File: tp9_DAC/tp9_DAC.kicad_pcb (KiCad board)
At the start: 2 copper layers, 24 parts, among them J2 BAT1, U1 NE555P, U2 NE555P

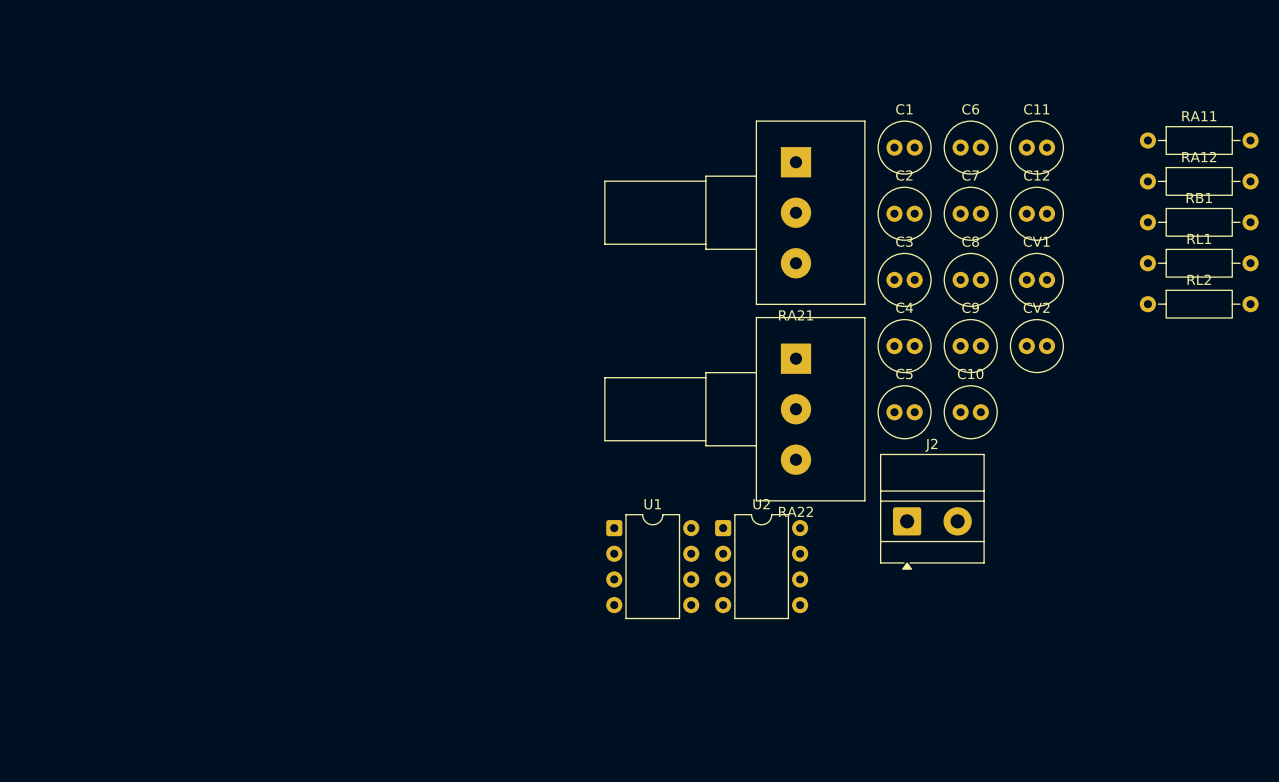
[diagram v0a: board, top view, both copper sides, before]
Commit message: update_tp9_DAC
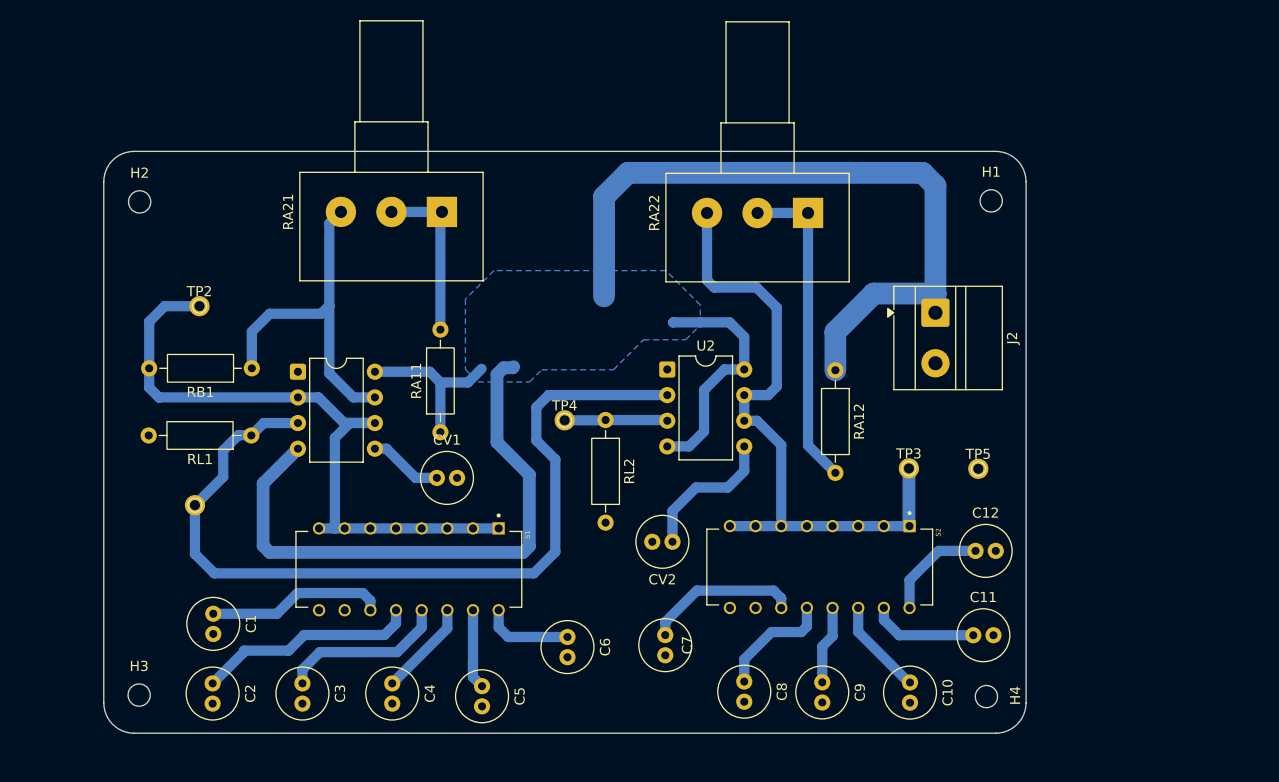
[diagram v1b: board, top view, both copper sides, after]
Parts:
- added H1: MountingHole, MountingHole:MountingHole_2.2mm_M2_DIN965, F.Cu at (168.8, 57.3)
- added H2: MountingHole, MountingHole:MountingHole_2.2mm_M2_DIN965, F.Cu at (84.5, 57.4)
- added H3: MountingHole, MountingHole:MountingHole_2.2mm_M2_DIN965, F.Cu at (84.5, 106.2)
- added H4: MountingHole, MountingHole:MountingHole_2.2mm_M2_DIN965, F.Cu at (168.3, 106.3)
- added S1: ADE0804, ADE0804:SW_ADE0804, F.Cu at (111.2, 93.8)
- added S2: ADE0804, ADE0804:SW_ADE0804, F.Cu at (151.8, 93.5)
- added TP1: TestPoint, TestPoint:TestPoint_THTPad_D1.0mm_Drill0.5mm, F.Cu at (90.0, 87.4)
- added TP2: TestPoint, TestPoint:TestPoint_THTPad_D1.0mm_Drill0.5mm, F.Cu at (90.5, 67.7)
- added TP3: TestPoint, TestPoint:TestPoint_THTPad_D1.0mm_Drill0.5mm, F.Cu at (160.7, 83.8)
- added TP4: TestPoint, TestPoint:TestPoint_THTPad_D1.0mm_Drill0.5mm, F.Cu at (126.6, 79.0)
- added TP5: TestPoint, TestPoint:TestPoint_THTPad_D1.0mm_Drill0.5mm, F.Cu at (167.6, 83.8)
- moved RL1 90.4 mm to (95.6, 80.5), turned to 180 degrees
- moved RB1 89.9 mm to (95.6, 73.8), turned to 180 degrees
- moved C2 82.0 mm to (91.8, 105.0), turned to -90 degrees
- moved C1 81.7 mm to (91.8, 98.2), turned to -90 degrees
- moved RA11 75.8 mm to (114.3, 80.2), turned to 90 degrees
- moved C3 70.9 mm to (100.6, 105.0), turned to -90 degrees
- moved C6 62.1 mm to (126.9, 100.4), turned to -90 degrees
- moved CV1 61.6 mm to (114.0, 84.7)
- moved C4 59.9 mm to (109.5, 105.0), turned to -90 degrees
- moved RL2 54.9 mm to (130.7, 79.0), turned to -90 degrees
- moved C7 50.9 mm to (136.6, 100.3), turned to -90 degrees
- moved C5 49.0 mm to (118.4, 105.3), turned to -90 degrees
- moved C11 48.6 mm to (167.1, 100.3)
- moved C8 45.2 mm to (144.4, 104.9), turned to -90 degrees
- moved CV2 40.1 mm to (137.3, 91.0), turned to 180 degrees
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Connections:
- C1 pad 1: unconnected-(C1-Pad1) -> Net-(C1-Pad1)
- C1 pad 2: unconnected-(C1-Pad2) -> GND
- C10 pad 1: unconnected-(C10-Pad1) -> Net-(C10-Pad1)
- C10 pad 2: unconnected-(C10-Pad2) -> GND
- C11 pad 1: unconnected-(C11-Pad1) -> Net-(C11-Pad1)
- C11 pad 2: unconnected-(C11-Pad2) -> GND
- C12 pad 1: unconnected-(C12-Pad1) -> Net-(C12-Pad1)
- C12 pad 2: unconnected-(C12-Pad2) -> GND
- C2 pad 1: unconnected-(C2-Pad1) -> Net-(C2-Pad1)
- C2 pad 2: unconnected-(C2-Pad2) -> GND
- C3 pad 1: unconnected-(C3-Pad1) -> Net-(C3-Pad1)
- C3 pad 2: unconnected-(C3-Pad2) -> GND
- C4 pad 1: unconnected-(C4-Pad1) -> Net-(C4-Pad1)
- C4 pad 2: unconnected-(C4-Pad2) -> GND
- C5 pad 1: unconnected-(C5-Pad1) -> Net-(C5-Pad1)
- C5 pad 2: unconnected-(C5-Pad2) -> GND
- C6 pad 1: unconnected-(C6-Pad1) -> Net-(C6-Pad1)
- C6 pad 2: unconnected-(C6-Pad2) -> GND
- C7 pad 1: unconnected-(C7-Pad1) -> Net-(C7-Pad1)
- C7 pad 2: unconnected-(C7-Pad2) -> GND
- C8 pad 1: unconnected-(C8-Pad1) -> Net-(C8-Pad1)
- C8 pad 2: unconnected-(C8-Pad2) -> GND
- C9 pad 1: unconnected-(C9-Pad1) -> Net-(C9-Pad1)
- C9 pad 2: unconnected-(C9-Pad2) -> GND
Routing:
- net +12V: track 0.00 -> 171.1 mm
- net Net-(U1-Q): track 0.00 -> 85.9 mm
- net Net-(U1-THR): track 0.00 -> 67.3 mm
- net Net-(U2-DIS): track 0.00 -> 65.0 mm
- net Net-(U1-DIS): track 0.00 -> 34.3 mm
- net Net-(RA12-Pad2): track 0.00 -> 31.8 mm
- net Net-(C2-Pad1): track 0.00 -> 22.0 mm
- net Net-(C1-Pad1): track 0.00 -> 17.7 mm
- net Net-(RA11-Pad2): track 0.00 -> 16.7 mm
- net Net-(C3-Pad1): track 0.00 -> 16.6 mm
- net Net-(C7-Pad1): track 0.00 -> 15.3 mm
- net Net-(U2-CV): track 0.00 -> 14.2 mm
- net Net-(C8-Pad1): track 0.00 -> 11.6 mm
- net Net-(C11-Pad1): track 0.00 -> 10.7 mm
- net Net-(C12-Pad1): track 0.00 -> 10.5 mm
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- added copper zone on B.Cu, net +12V
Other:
- board outline added: 91.3 x 57.6 mm

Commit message: update_tp9_pcb
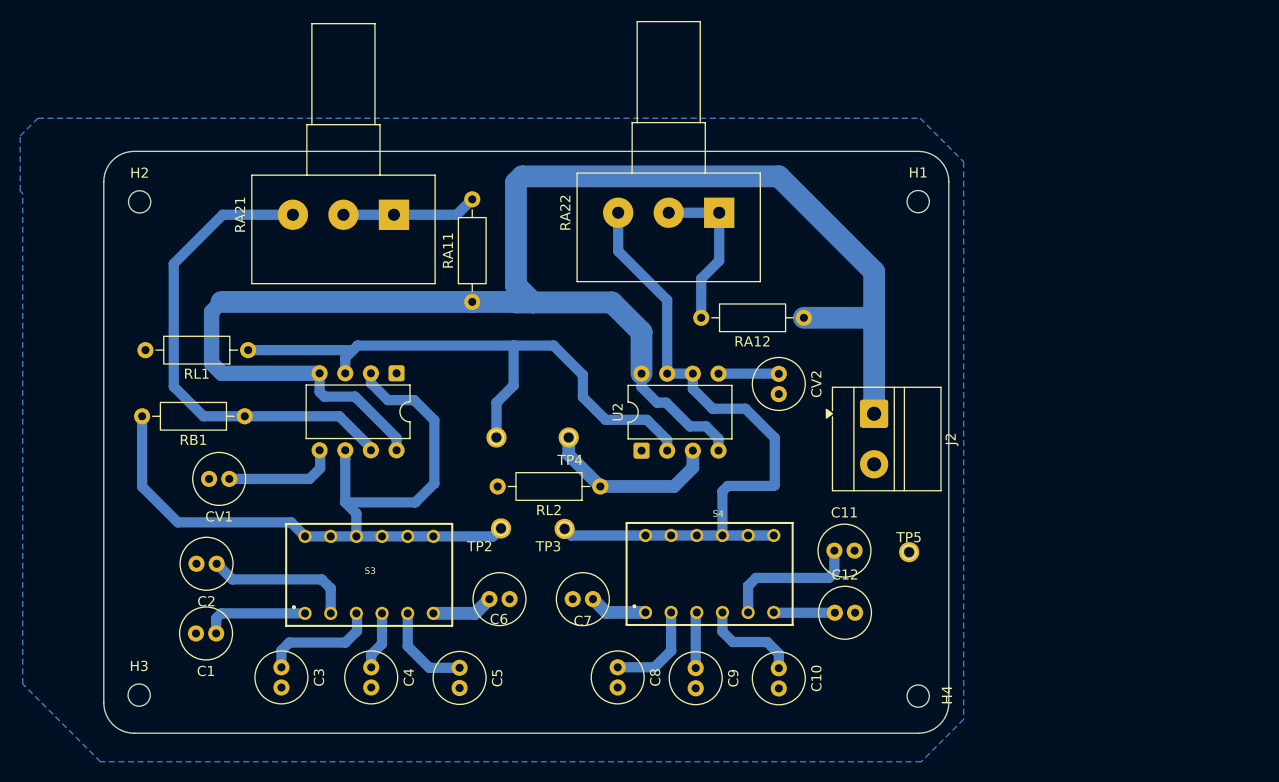
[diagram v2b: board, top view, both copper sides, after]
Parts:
- removed S1, S2: ADE0804, ADE0804:SW_ADE0804
- added S3: 418117270906, 418117270906:418117270906, F.Cu at (107.2, 94.3)
- added S4: 418117270906, 418117270906:418117270906, F.Cu at (140.9, 94.2)
- moved TP2 37.1 mm to (120.3, 89.7)
- moved TP3 34.6 mm to (126.6, 89.8)
- moved TP1 30.6 mm to (119.8, 80.7)
- moved CV1 20.6 mm to (93.4, 84.8), turned to 180 degrees
- moved CV2 19.7 mm to (147.8, 74.4), turned to -90 degrees
- moved C11 16.1 mm to (153.3, 91.9)
- moved C12 15.2 mm to (153.3, 98.0)
- moved RA11 13.3 mm to (117.5, 67.3)
- moved C10 13.1 mm to (147.8, 103.5)
- moved C8 12.6 mm to (131.8, 103.5)
- moved C9 12.6 mm to (139.6, 103.5)
- moved C2 11.9 mm to (92.2, 93.2), turned to 180 degrees
- moved J2 11.7 mm to (157.2, 78.3)
- moved TP5 10.7 mm to (160.7, 92.0)
- moved U1 9.77 mm to (110.0, 74.3), turned to -90 degrees
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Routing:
- net Net-(U1-Q): track 85.9 -> 60.3 mm
- net Net-(RA12-Pad2): track 31.8 -> 16.1 mm
- net Net-(U1-DIS): track 34.3 -> 48.2 mm
- net Net-(U1-THR): track 67.3 -> 78.5 mm
- net Net-(C7-Pad1): track 15.3 -> 5.75 mm
- net +12V: track 171.1 -> 162.5 mm
- net Net-(U2-CV): track 14.2 -> 5.98 mm
- net Net-(U2-Q): track 10.2 -> 17.8 mm
- net Net-(C2-Pad1): track 22.0 -> 14.8 mm
- net Net-(C1-Pad1): track 17.7 -> 10.5 mm
- net Net-(C3-Pad1): track 16.6 -> 11.7 mm
- net Net-(C12-Pad1): track 10.5 -> 6.06 mm
- net Net-(U1-CV): track 7.33 -> 11.2 mm
- net Net-(C4-Pad1): track 9.50 -> 5.78 mm
- net Net-(RA11-Pad2): track 16.7 -> 13.4 mm
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- added copper zone on B.Cu, net GND
- removed copper zone on B.Cu, net +12V
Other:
- board size 91.3 x 57.6 mm -> 83.7 x 57.6 mm

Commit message: modelos_step
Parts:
- moved J2 5.14 mm to (159.0, 83.2), turned to 90 degrees
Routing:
- net +12V: track 162.5 -> 172.1 mm
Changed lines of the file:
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@@
 			(psa4output no)
 			(plot_black_and_white yes)
-			(plotinvisibletext no)
 			(sketchpadsonfab no)
 			(plotpadnumbers no)
@@
 	(footprint "TerminalBlock_MetzConnect:TerminalBlock_MetzConnect_Type011_RT05502HBLC_1x02_P5.00mm_Horizontal"
 		(layer "F.Cu")
-		(at 157.2325 78.35 -90)
+		(at 158.9925 83.175 90)
 		(descr "terminal block Metz Connect Type011_RT05502HBLC, 2 pins, pitch 5mm, size 10x10.5mm, drill diameter 1.4mm, pad diameter 2.8mm, https://americancableassemblies.com/content/metz/863188.PDF, script-generated using https://gitlab.com/kicad/libraries/kicad-footprint-generator/-/tree/master/scripts/TerminalBlock_MetzConnect")
 		(tags "THT terminal block Metz Connect Type011_RT05502HBLC pitch 5mm size 10x10.5mm drill 1.4mm pad 2.8mm")
@@
 		(attr through_hole)
 		(fp_line
-			(start -2.62 4.12)
-			(end -2.62 -6.62)
+			(start 7.62 -6.62)
+			(end 7.62 4.12)
 			(stroke
 				(width 0.12)
@@
 		)
 		(fp_line
-			(start -0.3 4.12)
-			(end -2.62 4.12)
+			(start -2.62 -6.62)
+			(end 7.62 -6.62)
 			(stroke
 				(width 0.12)
@@
 		)
 		(fp_line
-			(start 7.62 4.12)
-			(end 0.3 4.12)
+			(start -2.62 -3)
+			(end 7.62 -3)
 			(stroke
 				(width 0.12)
@@
 		)
 		(fp_line
-			(start -2.62 2)
-			(end 7.62 2)
+			(start -2.62 -2)
+			(end 7.62 -2)
 			(stroke
 				(width 0.12)
@@
 		)
 		(fp_line
-			(start -2.62 -2)
-			(end 7.62 -2)
+			(start -2.62 2)
+			(end 7.62 2)
 			(stroke
 				(width 0.12)
@@
 		)
 		(fp_line
-			(start -2.62 -3)
-			(end 7.62 -3)
+			(start 7.62 4.12)
+			(end 0.3 4.12)
 			(stroke
 				(width 0.12)
@@
 		)
 		(fp_line
-			(start -2.62 -6.62)
-			(end 7.62 -6.62)
+			(start -0.3 4.12)
+			(end -2.62 4.12)
 			(stroke
 				(width 0.12)
@@
 		)
 		(fp_line
-			(start 7.62 -6.62)
-			(end 7.62 4.12)
+			(start -2.62 4.12)
+			(end -2.62 -6.62)
 			(stroke
 				(width 0.12)
@@
 		)
 		(fp_line
-			(start -3 4.5)
-			(end 8 4.5)
+			(start 8 -7)
+			(end -3 -7)
 			(stroke
 				(width 0.05)
@@
 		)
 		(fp_line
-			(start 8 4.5)
-			(end 8 -7)
+			(start -3 -7)
+			(end -3 4.5)
 			(stroke
 				(width 0.05)
@@
 		)
 		(fp_line
-			(start -3 -7)
-			(end -3 4.5)
+			(start 8 4.5)
+			(end 8 -7)
 			(stroke
 				(width 0.05)
@@
 		)
 		(fp_line
-			(start 8 -7)
-			(end -3 -7)
+			(start -3 4.5)
+			(end 8 4.5)
 			(stroke
 				(width 0.05)
@@
 		)
 		(fp_line
-			(start -0.5 4)
-			(end -2.5 2)
+			(start 7.5 -6.5)
+			(end 7.5 4)
 			(stroke
 				(width 0.1)
@@
 		)
 		(fp_line
-			(start 7.5 4)
-			(end -0.5 4)
+			(start -2.5 -6.5)
+			(end 7.5 -6.5)
 			(stroke
 				(width 0.1)
@@
 		)
 		(fp_line
-			(start -2.5 2)
-			(end 7.5 2)
+			(start -2.5 -3)
+			(end 7.5 -3)
 			(stroke
 				(width 0.1)
@@
 		)
 		(fp_line
-			(start -2.5 2)
-			(end -2.5 -6.5)
+			(start -2.5 -2)
+			(end 7.5 -2)
 			(stroke
 				(width 0.1)
@@
 		)
 		(fp_line
-			(start 1.213 -1.018)
-			(end -1.018 1.213)
+			(start 6.018 -1.213)
+			(end 3.787 1.018)
 			(stroke
 				(width 0.1)
@@
 		)
 		(fp_line
-			(start 6.213 -1.018)
-			(end 3.982 1.213)
+			(start 1.018 -1.213)
+			(end -1.213 1.018)
 			(stroke
 				(width 0.1)
@@
 		)
 		(fp_line
-			(start 1.018 -1.213)
-			(end -1.213 1.018)
+			(start 6.213 -1.018)
+			(end 3.982 1.213)
 			(stroke
 				(width 0.1)
@@
 		)
 		(fp_line
-			(start 6.018 -1.213)
-			(end 3.787 1.018)
+			(start 1.213 -1.018)
+			(end -1.018 1.213)
 			(stroke
 				(width 0.1)
@@
 		)
 		(fp_line
-			(start -2.5 -2)
-			(end 7.5 -2)
+			(start -2.5 2)
+			(end -2.5 -6.5)
 			(stroke
 				(width 0.1)
@@
 		)
 		(fp_line
-			(start -2.5 -3)
-			(end 7.5 -3)
+			(start -2.5 2)
+			(end 7.5 2)
 			(stroke
 				(width 0.1)
@@
 		)
 		(fp_line
-			(start -2.5 -6.5)
-			(end 7.5 -6.5)
+			(start 7.5 4)
+			(end -0.5 4)
 			(stroke
 				(width 0.1)
@@
 		)
 		(fp_line
-			(start 7.5 -6.5)
-			(end 7.5 4)
+			(start -0.5 4)
+			(end -2.5 2)
 			(stroke
 				(width 0.1)
@@
 		)
 		(fp_circle
-			(center 0 0)
-			(end 1.6 0)
+			(center 5 0)
+			(end 6.6 0)
 			(stroke
 				(width 0.1)
@@
 		)
 		(fp_circle
-			(center 5 0)
-			(end 6.6 0)
+			(center 0 0)
+			(end 1.6 0)
 			(stroke
 				(width 0.1)
@@
 		)
 		(pad "1" thru_hole roundrect
-			(at 0 0 270)
+			(at 0 0 90)
 			(size 2.8 2.8)
 			(drill 1.4)
@@
 		)
 		(pad "2" thru_hole circle
-			(at 5 0 270)
+			(at 5 0 90)
 			(size 2.8 2.8)
 			(drill 1.4)
@@
 			)
 		)
+		(model "${KICAD9_3DMODEL_DIR}/bornera_2pines.STEP"
+			(offset
+				(xyz 2.5 0.5 0)
+			)
+			(scale
+				(xyz 1 1 1)
+			)
+			(rotate
+				(xyz -90 -0 -0)
+			)
+		)
 	)
 	(footprint "Capacitor_THT:C_Radial_D5.0mm_H11.0mm_P2.00mm"
@@
 			)
 		)
+		(model "E:/Facultad-UNT/DAC/kicad_projects/lib_personal/dipswitch_6pos/dip_sw_6pos.step"
+			(offset
+				(xyz 0 0 0)
+			)
+			(scale
+				(xyz 1 1 1)
+			)
+			(rotate
+				(xyz -90 -0 -0)
+			)
+		)
 	)
 	(footprint "Capacitor_THT:C_Radial_D5.0mm_H11.0mm_P2.00mm"
@@
 			)
 		)
+		(model "E:/Facultad-UNT/DAC/kicad_projects/lib_personal/dipswitch_6pos/dip_sw_6pos.step"
+			(offset
+				(xyz 0 0 0)
+			)
+			(scale
+				(xyz 1 1 1)
+			)
+			(rotate
+				(xyz -90 -0 -0)
+			)
+		)
 	)
 	(footprint "Potentiometer_THT:Potentiometer_Alps_RK163_Single_Horizontal"
@@
 			)
 		)
+		(model "E:/Facultad-UNT/DAC/kicad_projects/lib_personal/Potentiometer.stp"
+			(offset
+				(xyz 5.5 -5 13)
+			)
+			(scale
+				(xyz 1 1 1)
+			)
+			(rotate
+				(xyz -0 180 90)
+			)
+		)
 	)
 	(footprint "Capacitor_THT:C_Radial_D5.0mm_H11.0mm_P2.00mm"
@@
 			)
 		)
+		(model "E:/Facultad-UNT/DAC/kicad_projects/lib_personal/Potentiometer.stp"
+			(offset
+				(xyz 5.5 -5 14)
+			)
+			(scale
+				(xyz 1 1 1)
+			)
+			(rotate
+				(xyz -180 -0 -90)
+			)
+		)
 	)
 	(footprint "Capacitor_THT:C_Radial_D5.0mm_H11.0mm_P2.00mm"
@@
 	)
 	(segment
+		(start 155.15 81.625)
+		(end 155.15 72.8)
+		(width 2.159)
+		(layer "B.Cu")
+		(net 4)
+	)
+	(segment
 		(start 122.4 54.85)
 		(end 121.78 55.47)
@@
 	)
 	(segment
+		(start 151.48 67.65)
+		(end 155.9825 67.65)
+		(width 2.159)
+		(layer "B.Cu")
+		(net 4)
+	)
+	(segment
 		(start 141.83 80.83)
 		(end 140.6 79.6)
@@
 	)
 	(segment
-		(start 150.28 68.85)
-		(end 157.1825 68.85)
+		(start 155.15 72.8)
+		(end 157.1825 70.7675)
 		(width 2.159)
 		(layer "B.Cu")
@@
 	)
 	(segment
-		(start 105.85 76.65)
-		(end 109.96 80.76)
-		(width 1.016)
+		(start 157.1825 70.7675)
+		(end 157.1825 68.85)
+		(width 2.159)
 		(layer "B.Cu")
 		(net 4)
 	)
 	(segment
-		(start 157.2325 78.35)
-		(end 157.2325 68.8)
-		(width 2.159)
+		(start 105.85 76.65)
+		(end 109.96 80.76)
+		(width 1.016)
 		(layer "B.Cu")
 		(net 4)
@@
 	)
 	(segment
+		(start 150.28 68.85)
+		(end 151.48 67.65)
+		(width 2.159)
+		(layer "B.Cu")
+		(net 4)
+	)
+	(segment
 		(start 131.28 67.33)
 		(end 134.21 70.26)
@@
 	)
 	(segment
+		(start 156.7 83.175)
+		(end 155.15 81.625)
+		(width 2.159)
+		(layer "B.Cu")
+		(net 4)
+	)
+	(segment
 		(start 102.8 76.65)
 		(end 105.85 76.65)
@@
 		(layer "B.Cu")
 		(net 4)
+	)
+	(segment
+		(start 158.9925 83.175)
+		(end 156.7 83.175)
+		(width 2.159)
+		(layer "B.Cu")
+		(net 4)
+	)
+	(segment
+		(start 155.9825 67.65)
+		(end 157.1825 68.85)
+		(width 2.159)
+		(layer "B.Cu")
+		(net 4)
